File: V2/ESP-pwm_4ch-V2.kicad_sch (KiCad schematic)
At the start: 33 parts

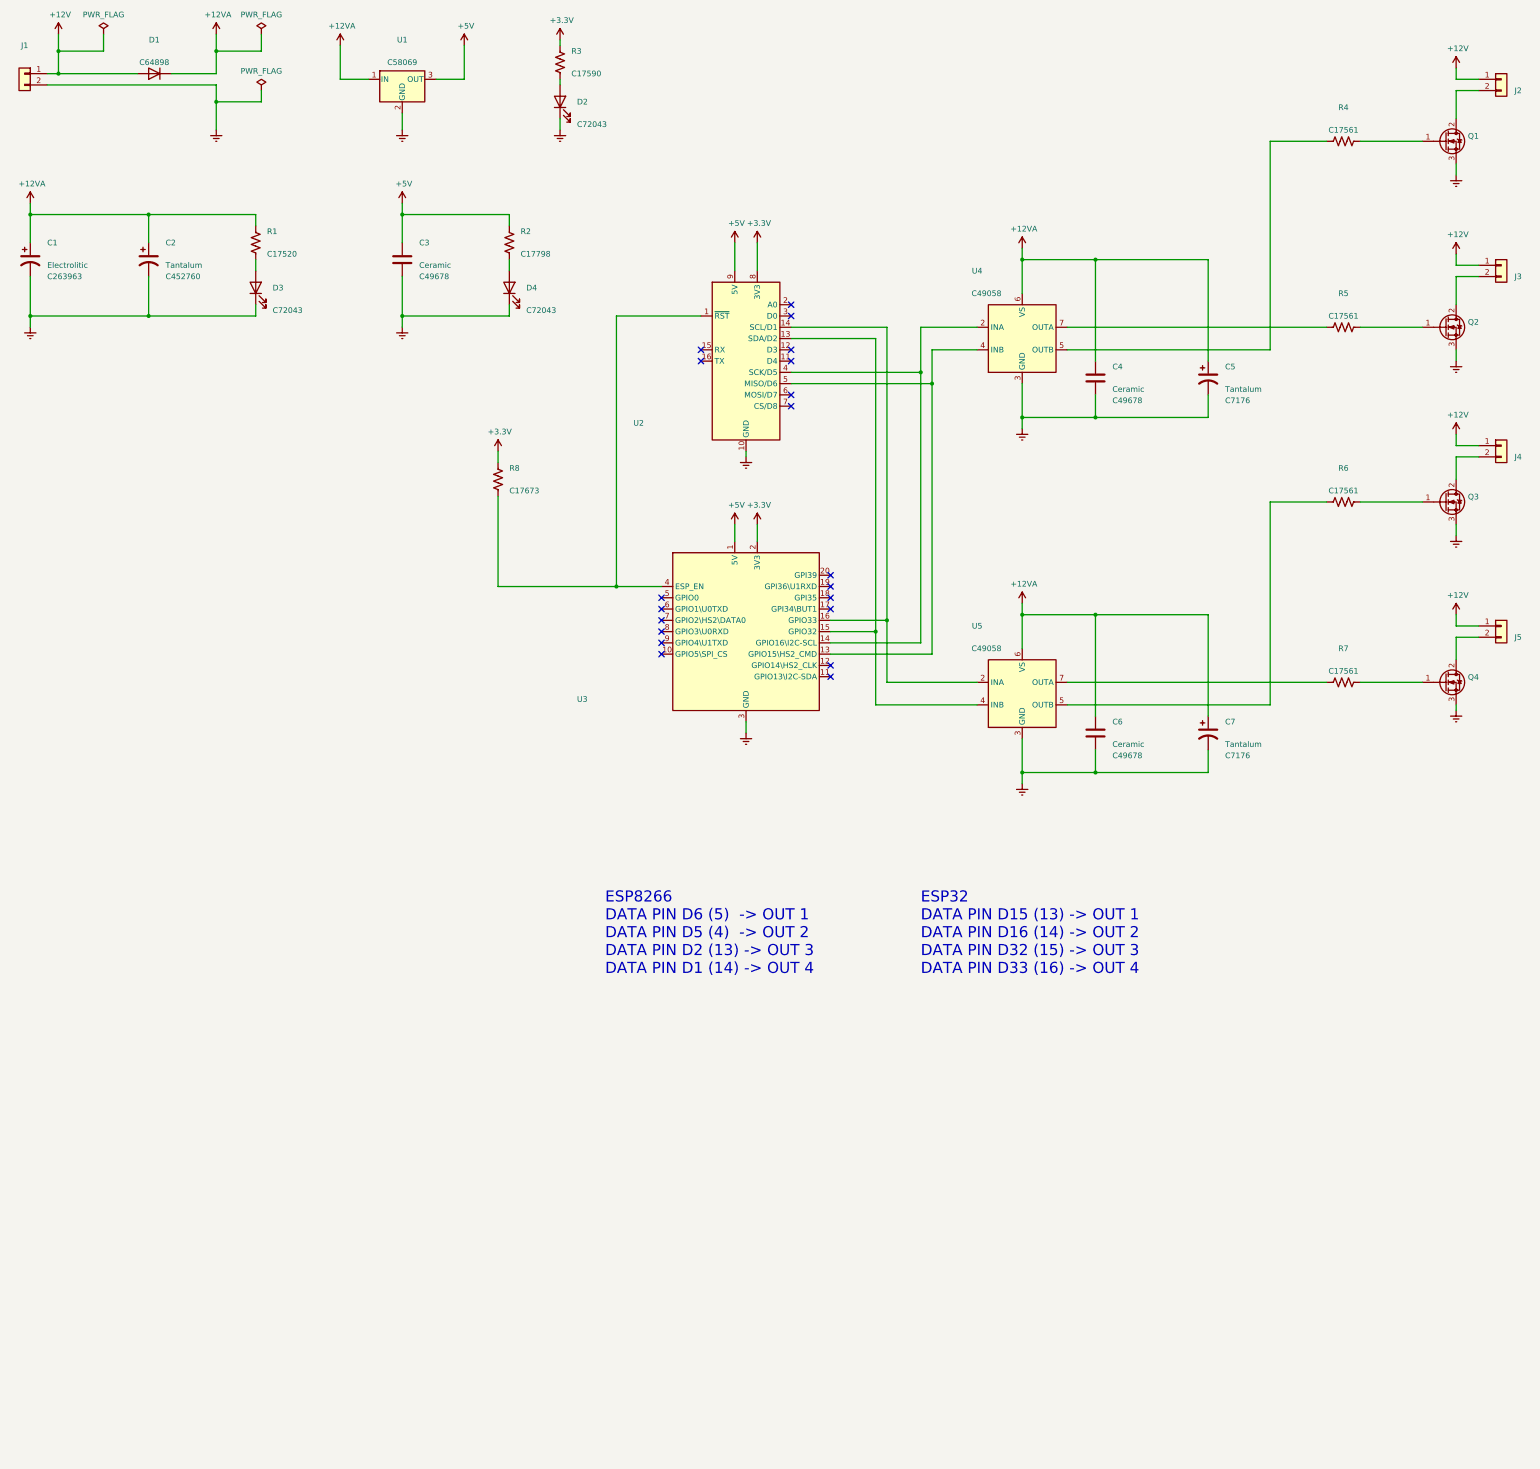
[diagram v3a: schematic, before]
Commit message: Tweaking footprints
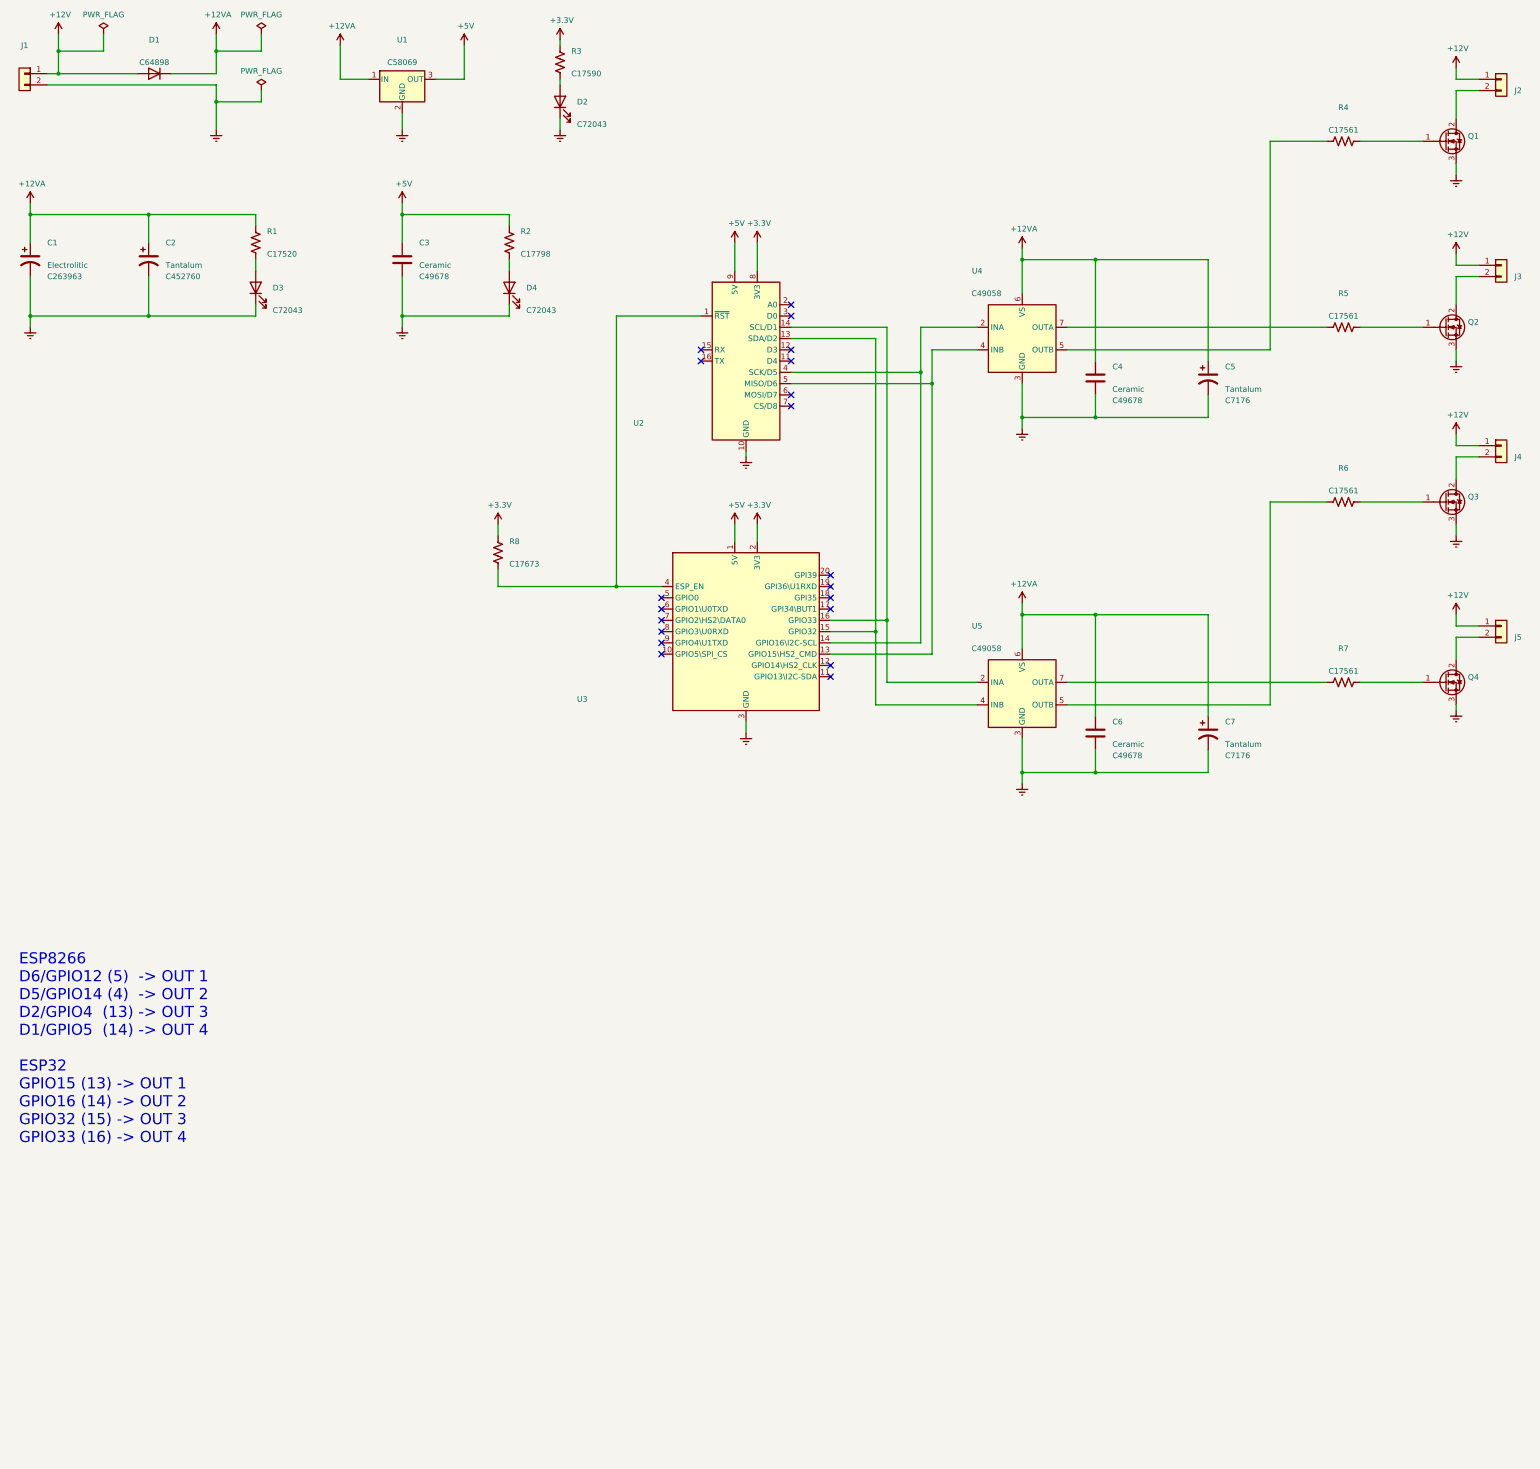
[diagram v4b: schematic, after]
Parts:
- C1, C2, C5, C7: symbol Device:CP1 -> Device:C_Polarized_US
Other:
- note added: "ESP8266 D6/GPIO12 (5) -> OUT 1 D5/GPIO14 (4) -> OUT 2 D2/GPIO4 (13) -> OUT 3 D1/GPIO5 (14) -> OUT 4 ESP32 GPIO15 (13) -> OUT 1 GPIO16 (14) -> OUT 2 GPIO32 (15) -> OUT 3 GPIO33 (16) -> OUT 4"
- note removed: "ESP32 DATA PIN D15 (13) -> OUT 1 DATA PIN D16 (14) -> OUT 2 DATA PIN D32 (15) -> OUT 3 DATA PIN D33 (16) -> OUT 4"
- note removed: "ESP8266 DATA PIN D6 (5) -> OUT 1 DATA PIN D5 (4) -> OUT 2 DATA PIN D2 (13) -> OUT 3 DATA PIN D1 (14) -> OUT 4"
- moved on the sheet: R8
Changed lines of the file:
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@@
     (stroke (width 0) (type default) (color 0 0 0 0))
   )
-  (wire (pts (xy 130.81 129.54) (xy 130.81 149.86))
+  (wire (pts (xy 130.81 146.05) (xy 130.81 149.86))
     (stroke (width 0) (type default) (color 0 0 0 0))
   )
@@
     (stroke (width 0) (type default) (color 0 0 0 0))
   )
-  (wire (pts (xy 130.81 119.38) (xy 130.81 121.92))
+  (wire (pts (xy 130.81 135.89) (xy 130.81 138.43))
     (stroke (width 0) (type default) (color 0 0 0 0))
   )
@@
     (stroke (width 0) (type default) (color 0 0 0 0))
   )
-  (text "ESP32\nDATA PIN D15 (13) -> OUT 1\nDATA PIN D16 (14) -> OUT 2\nDATA PIN D32 (15) -> OUT 3\nDATA PIN D33 (16) -> OUT 4"
-    (at 226.06 237.49 0)
-    (effects (font (size 2.5 2.5)) (justify left bottom))
-  )
-  (text "ESP8266\nDATA PIN D6 (5)  -> OUT 1\nDATA PIN D5 (4)  -> OUT 2\nDATA PIN D2 (13) -> OUT 3\nDATA PIN D1 (14) -> OUT 4"
-    (at 154.94 237.49 0)
+  (text "ESP8266\nD6/GPIO12 (5)  -> OUT 1\nD5/GPIO14 (4)  -> OUT 2\nD2/GPIO4  (13) -> OUT 3\nD1/GPIO5  (14) -> OUT 4\n\nESP32\nGPIO15 (13) -> OUT 1\nGPIO16 (14) -> OUT 2\nGPIO32 (15) -> OUT 3\nGPIO33 (16) -> OUT 4"
+    (at 22.86 275.59 0)
     (effects (font (size 2.5 2.5)) (justify left bottom))
   )
@@
     (pin "2")
   )
-  (symbol (lib_id "Device:CP1") (at 290.83 102.87 0) (unit 1)
+  (symbol (lib_id "Device:C_Polarized_US") (at 290.83 102.87 0) (unit 1)
     (in_bom yes) (on_board yes)
     (property "Reference" "C5" (id 0) (at 294.64 100.33 0)
@@
     (pin "2")
   )
-  (symbol (lib_id "Device:CP1") (at 290.83 182.88 0) (unit 1)
+  (symbol (lib_id "Device:C_Polarized_US") (at 290.83 182.88 0) (unit 1)
     (in_bom yes) (on_board yes)
     (property "Reference" "C7" (id 0) (at 294.64 180.34 0)
@@
     (pin "1")
   )
-  (symbol (lib_id "Device:CP1") (at 52.07 76.2 0) (unit 1)
+  (symbol (lib_id "Device:C_Polarized_US") (at 52.07 76.2 0) (unit 1)
     (in_bom yes) (on_board yes)
     (property "Reference" "C2" (id 0) (at 55.88 72.39 0)
@@
     (pin "2")
   )
-  (symbol (lib_id "Device:CP1") (at 25.4 76.2 0) (unit 1)
+  (symbol (lib_id "Device:C_Polarized_US") (at 25.4 76.2 0) (unit 1)
     (in_bom yes) (on_board yes)
     (property "Reference" "C1" (id 0) (at 29.21 72.39 0)
@@
     (pin "1")
   )
-  (symbol (lib_id "Device:R_US") (at 130.81 125.73 0) (unit 1)
-    (in_bom yes) (on_board yes)
-    (property "Reference" "R8" (id 0) (at 133.35 123.19 0)
-      (effects (font (size 1.27 1.27)) (justify left))
-    )
-    (property "Value" "" (id 1) (at 133.35 125.73 0)
-      (effects (font (size 1.27 1.27)) (justify left))
-    )
-    (property "Footprint" "" (id 2) (at 131.826 125.984 90)
-      (effects (font (size 1.27 1.27)) hide)
-    )
-    (property "Datasheet" "~" (id 3) (at 130.81 125.73 0)
-      (effects (font (size 1.27 1.27)) hide)
-    )
-    (property "Case" "0805/2012" (id 4) (at 130.81 125.73 0)
-      (effects (font (size 1.27 1.27)) hide)
-    )
-    (property "Mfr" "Uniroyal" (id 5) (at 130.81 125.73 0)
-      (effects (font (size 1.27 1.27)) hide)
-    )
-    (property "Mfr PN" "0805W8F6800T5E" (id 6) (at 130.81 125.73 0)
-      (effects (font (size 1.27 1.27)) hide)
-    )
-    (property "Vendor" "JLCPCB" (id 7) (at 130.81 125.73 0)
-      (effects (font (size 1.27 1.27)) hide)
-    )
-    (property "Vendor PN" "C17673" (id 8) (at 130.81 125.73 0)
-      (effects (font (size 1.27 1.27)) hide)
-    )
-    (property "JLCPCB BOM" "1" (id 9) (at 130.81 125.73 0)
-      (effects (font (size 1.27 1.27)) hide)
-    )
-    (property "LCSC Part" "C17673" (id 10) (at 133.35 128.27 0)
-      (effects (font (size 1.27 1.27)) (justify left))
-    )
-    (pin "1")
-    (pin "2")
-  )
-  (symbol (lib_id "power:+3.3V") (at 130.81 119.38 0) (unit 1)
-    (in_bom yes) (on_board yes)
-    (property "Reference" "#PWR0121" (id 0) (at 130.81 123.19 0)
-      (effects (font (size 1.27 1.27)) hide)
-    )
-    (property "Value" "+3.3V" (id 1) (at 131.191 114.9858 0))
-    (property "Footprint" "" (id 2) (at 130.81 119.38 0)
-      (effects (font (size 1.27 1.27)) hide)
-    )
-    (property "Datasheet" "" (id 3) (at 130.81 119.38 0)
+  (symbol (lib_id "Device:R_US") (at 130.81 142.24 0) (unit 1)
+    (in_bom yes) (on_board yes)
+    (property "Reference" "R8" (id 0) (at 133.35 139.7 0)
+      (effects (font (size 1.27 1.27)) (justify left))
+    )
+    (property "Value" "" (id 1) (at 133.35 142.24 0)
+      (effects (font (size 1.27 1.27)) (justify left))
+    )
+    (property "Footprint" "" (id 2) (at 131.826 142.494 90)
+      (effects (font (size 1.27 1.27)) hide)
+    )
+    (property "Datasheet" "~" (id 3) (at 130.81 142.24 0)
+      (effects (font (size 1.27 1.27)) hide)
+    )
+    (property "Case" "0805/2012" (id 4) (at 130.81 142.24 0)
+      (effects (font (size 1.27 1.27)) hide)
+    )
+    (property "Mfr" "Uniroyal" (id 5) (at 130.81 142.24 0)
+      (effects (font (size 1.27 1.27)) hide)
+    )
+    (property "Mfr PN" "0805W8F6800T5E" (id 6) (at 130.81 142.24 0)
+      (effects (font (size 1.27 1.27)) hide)
+    )
+    (property "Vendor" "JLCPCB" (id 7) (at 130.81 142.24 0)
+      (effects (font (size 1.27 1.27)) hide)
+    )
+    (property "Vendor PN" "C17673" (id 8) (at 130.81 142.24 0)
+      (effects (font (size 1.27 1.27)) hide)
+    )
+    (property "JLCPCB BOM" "1" (id 9) (at 130.81 142.24 0)
+      (effects (font (size 1.27 1.27)) hide)
+    )
+    (property "LCSC Part" "C17673" (id 10) (at 133.35 144.78 0)
+      (effects (font (size 1.27 1.27)) (justify left))
+    )
+    (pin "1")
+    (pin "2")
+  )
+  (symbol (lib_id "power:+3.3V") (at 130.81 135.89 0) (unit 1)
+    (in_bom yes) (on_board yes)
+    (property "Reference" "#PWR0121" (id 0) (at 130.81 139.7 0)
+      (effects (font (size 1.27 1.27)) hide)
+    )
+    (property "Value" "+3.3V" (id 1) (at 131.191 131.4958 0))
+    (property "Footprint" "" (id 2) (at 130.81 135.89 0)
+      (effects (font (size 1.27 1.27)) hide)
+    )
+    (property "Datasheet" "" (id 3) (at 130.81 135.89 0)
       (effects (font (size 1.27 1.27)) hide)
     )
@@
     )
     (path "/00000000-0000-0000-0000-000061efe1bd"
-      (reference "Q1") (unit 1) (value "IRLB8721PBF") (footprint "Package_TO_SOT_THT:TO-220-3_Vertical")
+      (reference "Q1") (unit 1) (value "IRLB8721PBF") (footprint "Tales:TO-220-3_Vertical")
     )
     (path "/00000000-0000-0000-0000-0000615c309d"
-      (reference "Q2") (unit 1) (value "IRLB8721PBF") (footprint "Package_TO_SOT_THT:TO-220-3_Vertical")
+      (reference "Q2") (unit 1) (value "IRLB8721PBF") (footprint "Tales:TO-220-3_Vertical")
     )
     (path "/00000000-0000-0000-0000-0000615f02ef"
-      (reference "Q3") (unit 1) (value "IRLB8721PBF") (footprint "Package_TO_SOT_THT:TO-220-3_Vertical")
+      (reference "Q3") (unit 1) (value "IRLB8721PBF") (footprint "Tales:TO-220-3_Vertical")
     )
     (path "/00000000-0000-0000-0000-0000615f030d"
-      (reference "Q4") (unit 1) (value "IRLB8721PBF") (footprint "Package_TO_SOT_THT:TO-220-3_Vertical")
+      (reference "Q4") (unit 1) (value "IRLB8721PBF") (footprint "Tales:TO-220-3_Vertical")
     )
     (path "/00000000-0000-0000-0000-00006055f4b5"
@@
     )
     (path "/00000000-0000-0000-0000-0000614c0886"
-      (reference "U4") (unit 1) (value "IR4427") (footprint "Package_SO:SOIC-8_3.9x4.9mm_P1.27mm")
+      (reference "U4") (unit 1) (value "IR4427") (footprint "Tales:SOIC-8_3.9x4.9mm_P1.27mm")
     )
     (path "/00000000-0000-0000-0000-0000614c177b"
-      (reference "U5") (unit 1) (value "IR4427") (footprint "Package_SO:SOIC-8_3.9x4.9mm_P1.27mm")
-    )
-  )
+      (reference "U5") (unit 1) (value "IR4427") (footprint "Tales:SOIC-8_3.9x4.9mm_P1.27mm")
+    )
+  )
